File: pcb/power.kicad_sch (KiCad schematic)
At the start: 24 parts, among them J2 SM02B-SRSS-TB, Q1 2N7002, Q2 BSS84, SW1 SSSS211603, U2 TPS2112APW, U3 MCP73831-5-OT, U4 TLV70233DBVT

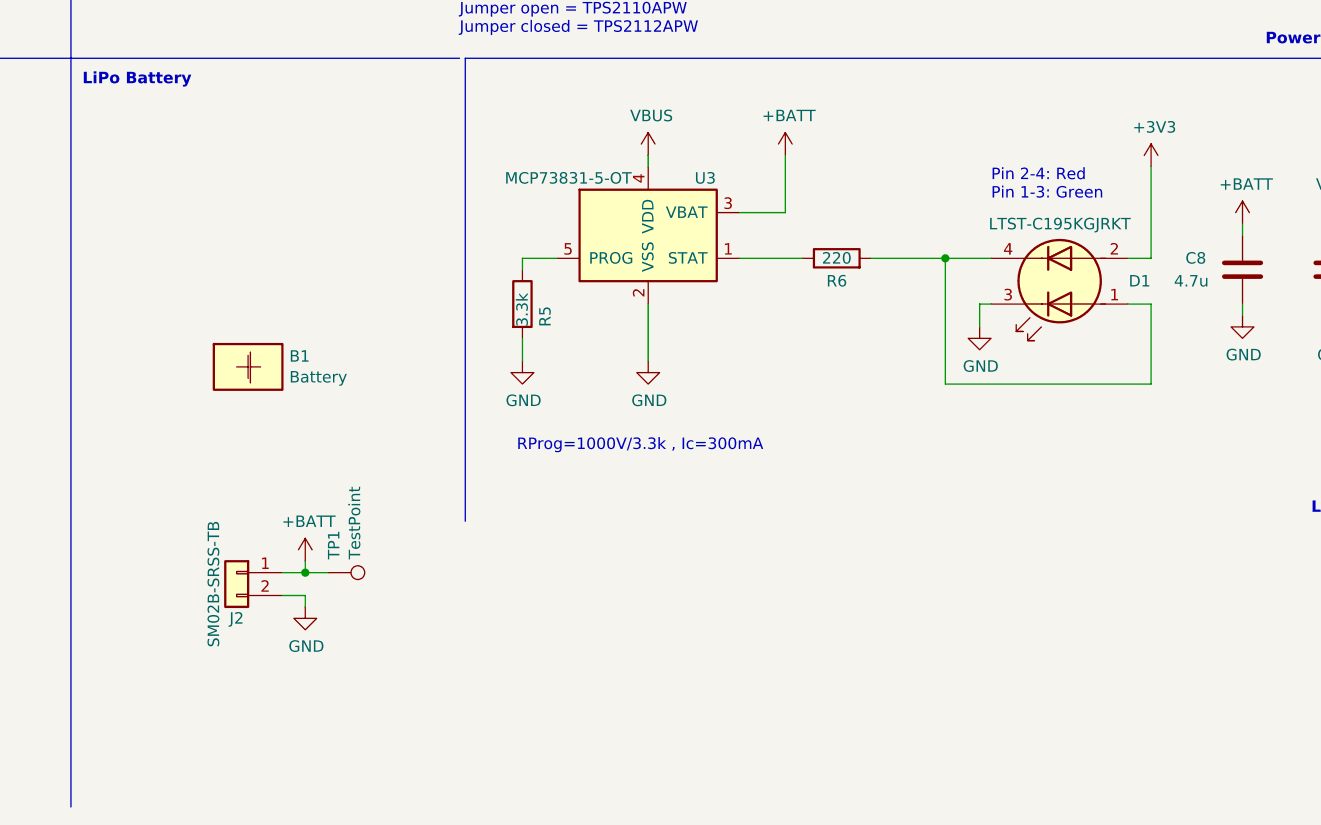
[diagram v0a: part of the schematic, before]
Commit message: Fix ERC warnings
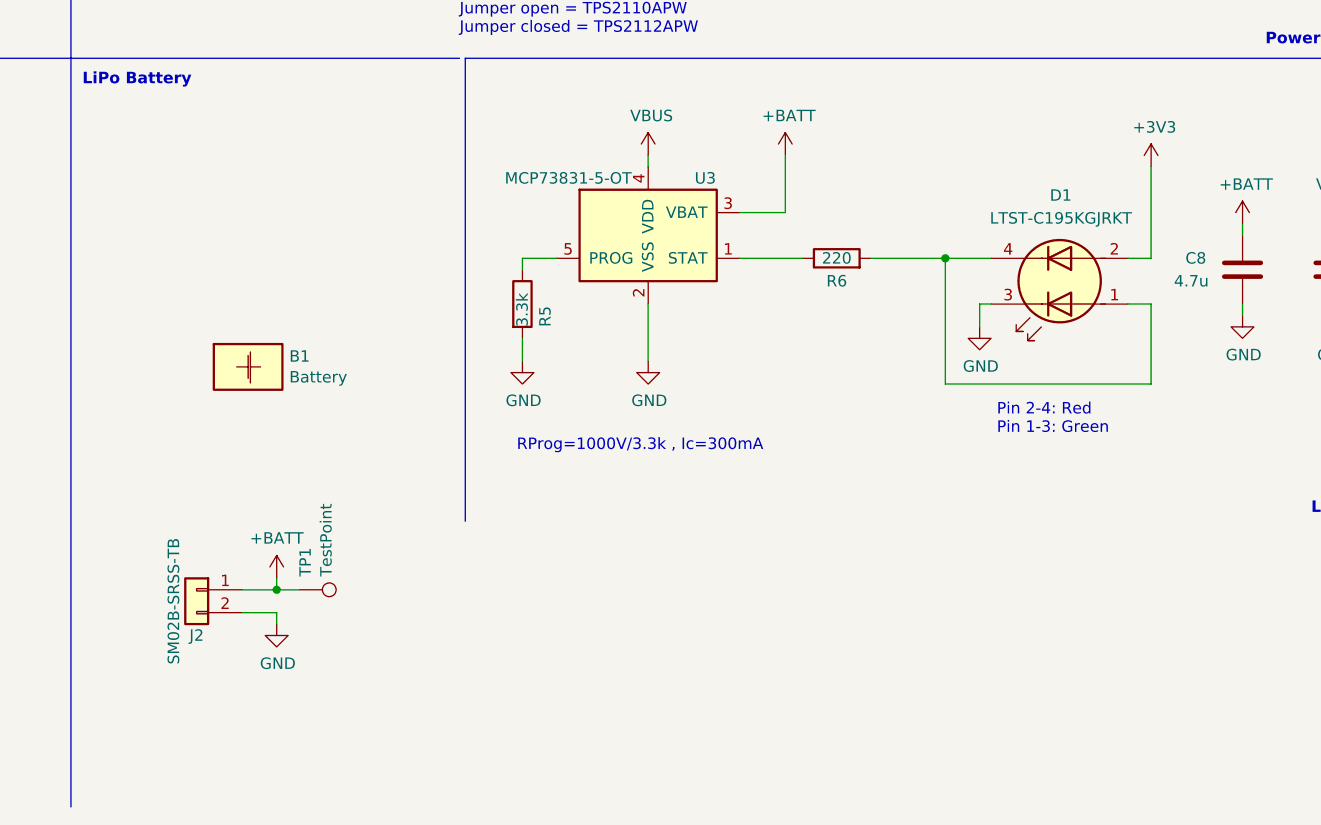
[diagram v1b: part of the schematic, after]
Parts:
- removed D1: LTST-C195KGJRKT, ultramote:LTST-C195KGJRKT, symbol ultramote-rescue:LED_Dual_AACC-Device
- added D1: LTST-C195KGJRKT, ultramote:LTST-C195KGJRKT, symbol Device:LED_Dual_AAKK
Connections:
- net +3V3: now also D1.2 (A2)
- net GND: now also D1.3 (K1)
- net at R6.2: now also D1.1 (A1), D1.4 (K2)
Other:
- moved on the sheet: J2, TP1
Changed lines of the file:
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@@
   (junction (at 189.23 73.66) (diameter 0) (color 0 0 0 0)
   )
-  (junction (at 159.385 171.45) (diameter 0) (color 0 0 0 0)
+  (junction (at 156.21 173.355) (diameter 0) (color 0 0 0 0)
   )
   (junction (at 144.78 53.34) (diameter 0) (color 0 0 0 0)
@@
   (junction (at 219.71 50.8) (diameter 0) (color 0 0 0 0)
   )
-  (wire (pts (xy 156.845 173.99) (xy 159.385 173.99))
+  (wire (pts (xy 152.4 175.895) (xy 156.21 175.895))
     (stroke (width 0) (type default) (color 0 0 0 0))
   )
@@
     (stroke (width 0) (type default) (color 0 0 0 0))
   )
-  (wire (pts (xy 159.385 171.45) (xy 156.845 171.45))
-    (stroke (width 0) (type default) (color 0 0 0 0))
-  )
   (wire (pts (xy 203.2 53.34) (xy 203.2 63.5))
     (stroke (width 0) (type default) (color 0 0 0 0))
@@
     (stroke (width 0) (type default) (color 0 0 0 0))
   )
+  (wire (pts (xy 152.4 173.355) (xy 156.21 173.355))
+    (stroke (width 0) (type default) (color 0 0 0 0))
+  )
   (wire (pts (xy 179.07 62.23) (xy 170.18 62.23))
     (stroke (width 0) (type default) (color 0 0 0 0))
@@
     (stroke (width 0) (type default) (color 0 0 0 0))
   )
-  (wire (pts (xy 161.925 171.45) (xy 159.385 171.45))
+  (wire (pts (xy 158.75 173.355) (xy 156.21 173.355))
     (stroke (width 0) (type default) (color 0 0 0 0))
   )
@@
     (stroke (width 0) (type default) (color 0 0 0 0))
   )
-  (wire (pts (xy 159.385 170.18) (xy 159.385 171.45))
+  (wire (pts (xy 156.21 172.085) (xy 156.21 173.355))
     (stroke (width 0) (type default) (color 0 0 0 0))
   )
@@
     (stroke (width 0) (type default) (color 0 0 0 0))
   )
-  (wire (pts (xy 159.385 173.99) (xy 159.385 175.26))
+  (wire (pts (xy 156.21 175.895) (xy 156.21 177.165))
     (stroke (width 0) (type default) (color 0 0 0 0))
   )
@@
     (effects (font (size 1.27 1.27) (thickness 0.254) bold) (justify left bottom))
   )
-  (text "Pin 2-4: Red\nPin 1-3: Green" (at 235.585 130.175 0)
+  (text "Pin 2-4: Red\nPin 1-3: Green" (at 236.22 156.21 0)
     (effects (font (size 1.27 1.27)) (justify left bottom))
   )
@@
     (pin "2")
   )
-  (symbol (lib_id "Connector_Generic:Conn_01x02") (at 151.765 171.45 0) (mirror y) (unit 1)
-    (in_bom yes) (on_board yes)
-    (property "Reference" "J2" (id 0) (at 151.765 176.53 0))
-    (property "Value" "SM02B-SRSS-TB" (id 1) (at 149.225 172.72 90))
-    (property "Footprint" "Connector_JST:JST_PH_B2B-PH-SM4-TB_1x02-1MP_P2.00mm_Vertical" (id 2) (at 151.765 171.45 0)
-      (effects (font (size 1.27 1.27)) hide)
-    )
-    (property "Datasheet" "~" (id 3) (at 151.765 171.45 0)
-      (effects (font (size 1.27 1.27)) hide)
-    )
-    (property "LCSC Part Number" "C160402" (id 4) (at 151.765 171.45 0)
-      (effects (font (size 1.27 1.27)) hide)
-    )
-    (property "Manufacturer Part Number" "S2B-PH-SM4-TB(LF)(SN)" (id 5) (at 151.765 171.45 0)
+  (symbol (lib_id "Connector_Generic:Conn_01x02") (at 147.32 173.355 0) (mirror y) (unit 1)
+    (in_bom yes) (on_board yes)
+    (property "Reference" "J2" (id 0) (at 147.32 178.435 0))
+    (property "Value" "SM02B-SRSS-TB" (id 1) (at 144.78 174.625 90))
+    (property "Footprint" "Connector_JST:JST_PH_B2B-PH-SM4-TB_1x02-1MP_P2.00mm_Vertical" (id 2) (at 147.32 173.355 0)
+      (effects (font (size 1.27 1.27)) hide)
+    )
+    (property "Datasheet" "~" (id 3) (at 147.32 173.355 0)
+      (effects (font (size 1.27 1.27)) hide)
+    )
+    (property "LCSC Part Number" "C160402" (id 4) (at 147.32 173.355 0)
+      (effects (font (size 1.27 1.27)) hide)
+    )
+    (property "Manufacturer Part Number" "S2B-PH-SM4-TB(LF)(SN)" (id 5) (at 147.32 173.355 0)
       (effects (font (size 1.27 1.27)) hide)
     )
@@
     )
     (pin "1")
-  )
-  (symbol (lib_id "ultramote-rescue:LED_Dual_AACC-Device") (at 243.205 139.065 180) (unit 1)
-    (in_bom yes) (on_board yes)
-    (property "Reference" "D1" (id 0) (at 252.095 139.065 0))
-    (property "Value" "LTST-C195KGJRKT" (id 1) (at 243.205 132.715 0))
-    (property "Footprint" "ultramote:LTST-C195KGJRKT" (id 2) (at 242.443 139.065 0)
-      (effects (font (size 1.27 1.27)) hide)
-    )
-    (property "Datasheet" "~" (id 3) (at 242.443 139.065 0)
-      (effects (font (size 1.27 1.27)) hide)
-    )
-    (property "LCSC Part Number" "C125104" (id 4) (at 243.205 139.065 0)
-      (effects (font (size 1.27 1.27)) hide)
-    )
-    (property "Manufacturer Part Number" "LTST-C195KGJRKT" (id 5) (at 243.205 139.065 0)
-      (effects (font (size 1.27 1.27)) hide)
-    )
-    (pin "1")
-    (pin "2")
-    (pin "3")
-    (pin "4")
   )
   (symbol (lib_id "power:+3V3") (at 254 48.26 0) (unit 1)
@@
     (pin "1")
   )
-  (symbol (lib_id "power:GND") (at 159.385 175.26 0) (unit 1)
-    (in_bom yes) (on_board yes)
-    (property "Reference" "#PWR018" (id 0) (at 159.385 181.61 0)
-      (effects (font (size 1.27 1.27)) hide)
-    )
-    (property "Value" "GND" (id 1) (at 159.512 179.6542 0))
-    (property "Footprint" "" (id 2) (at 159.385 175.26 0)
-      (effects (font (size 1.27 1.27)) hide)
-    )
-    (property "Datasheet" "" (id 3) (at 159.385 175.26 0)
+  (symbol (lib_id "power:GND") (at 156.21 177.165 0) (unit 1)
+    (in_bom yes) (on_board yes)
+    (property "Reference" "#PWR018" (id 0) (at 156.21 183.515 0)
+      (effects (font (size 1.27 1.27)) hide)
+    )
+    (property "Value" "GND" (id 1) (at 156.337 181.5592 0))
+    (property "Footprint" "" (id 2) (at 156.21 177.165 0)
+      (effects (font (size 1.27 1.27)) hide)
+    )
+    (property "Datasheet" "" (id 3) (at 156.21 177.165 0)
       (effects (font (size 1.27 1.27)) hide)
     )
@@
     )
     (pin "1")
+  )
+  (symbol (lib_id "Device:LED_Dual_AAKK") (at 243.205 139.065 180) (unit 1)
+    (in_bom yes) (on_board yes)
+    (property "Reference" "D1" (id 0) (at 243.332 129.54 0))
+    (property "Value" "LTST-C195KGJRKT" (id 1) (at 243.332 132.08 0))
+    (property "Footprint" "ultramote:LTST-C195KGJRKT" (id 2) (at 242.443 139.065 0)
+      (effects (font (size 1.27 1.27)) hide)
+    )
+    (property "Datasheet" "~" (id 3) (at 242.443 139.065 0)
+      (effects (font (size 1.27 1.27)) hide)
+    )
+    (property "LCSC Part Number" "C125104" (id 4) (at 243.205 139.065 0)
+      (effects (font (size 1.27 1.27)) hide)
+    )
+    (property "Manufacturer Part Number" "LTST-C195KGJRKT" (id 5) (at 243.205 139.065 0)
+      (effects (font (size 1.27 1.27)) hide)
+    )
+    (pin "1")
+    (pin "2")
+    (pin "3")
+    (pin "4")
   )
   (symbol (lib_id "Device:C") (at 74.93 162.56 0) (unit 1)
@@
     (pin "2")
   )
-  (symbol (lib_id "power:+BATT") (at 159.385 170.18 0) (unit 1)
-    (in_bom yes) (on_board yes)
-    (property "Reference" "#PWR017" (id 0) (at 159.385 173.99 0)
-      (effects (font (size 1.27 1.27)) hide)
-    )
-    (property "Value" "+BATT" (id 1) (at 159.766 165.7858 0))
-    (property "Footprint" "" (id 2) (at 159.385 170.18 0)
-      (effects (font (size 1.27 1.27)) hide)
-    )
-    (property "Datasheet" "" (id 3) (at 159.385 170.18 0)
+  (symbol (lib_id "power:+BATT") (at 156.21 172.085 0) (unit 1)
+    (in_bom yes) (on_board yes)
+    (property "Reference" "#PWR017" (id 0) (at 156.21 175.895 0)
+      (effects (font (size 1.27 1.27)) hide)
+    )
+    (property "Value" "+BATT" (id 1) (at 156.21 167.64 0))
+    (property "Footprint" "" (id 2) (at 156.21 172.085 0)
+      (effects (font (size 1.27 1.27)) hide)
+    )
+    (property "Datasheet" "" (id 3) (at 156.21 172.085 0)
       (effects (font (size 1.27 1.27)) hide)
     )
@@
     (pin "5")
   )
-  (symbol (lib_id "Connector:TestPoint") (at 161.925 171.45 270) (unit 1)
-    (in_bom yes) (on_board yes)
-    (property "Reference" "TP1" (id 0) (at 162.5854 169.9768 0)
+  (symbol (lib_id "Connector:TestPoint") (at 158.75 173.355 270) (unit 1)
+    (in_bom yes) (on_board yes)
+    (property "Reference" "TP1" (id 0) (at 159.4104 171.8818 0)
       (effects (font (size 1.27 1.27)) (justify right))
     )
-    (property "Value" "TestPoint" (id 1) (at 164.8968 169.9768 0)
+    (property "Value" "TestPoint" (id 1) (at 161.7218 171.8818 0)
       (effects (font (size 1.27 1.27)) (justify right))
     )
-    (property "Footprint" "TestPoint:TestPoint_Pad_1.0x1.0mm" (id 2) (at 161.925 176.53 0)
-      (effects (font (size 1.27 1.27)) hide)
-    )
-    (property "Datasheet" "~" (id 3) (at 161.925 176.53 0)
-      (effects (font (size 1.27 1.27)) hide)
-    )
+    (property "Footprint" "TestPoint:TestPoint_Pad_1.0x1.0mm" (id 2) (at 158.75 178.435 0)
+      (effects (font (size 1.27 1.27)) hide)
+    )
+    (property "Datasheet" "~" (id 3) (at 158.75 178.435 0)
+      (effects (font (size 1.27 1.27)) hide)
+    )

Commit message: Add datasheet links
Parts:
- J2: footprint Connector_JST:JST_PH_B2B-PH-SM4-TB_1x02-1MP_P2.00mm_Vertical -> Connector_JST:JST_SH_SM02B-SRSS-TB_1x02-1MP_P1.00mm_Horizontal
- U3: LCSC Part Number C424093 -> C424093
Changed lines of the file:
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@@
     (property "Reference" "J2" (id 0) (at 147.32 178.435 0))
     (property "Value" "SM02B-SRSS-TB" (id 1) (at 144.78 174.625 90))
-    (property "Footprint" "Connector_JST:JST_PH_B2B-PH-SM4-TB_1x02-1MP_P2.00mm_Vertical" (id 2) (at 147.32 173.355 0)
-      (effects (font (size 1.27 1.27)) hide)
-    )
-    (property "Datasheet" "~" (id 3) (at 147.32 173.355 0)
+    (property "Footprint" "Connector_JST:JST_SH_SM02B-SRSS-TB_1x02-1MP_P1.00mm_Horizontal" (id 2) (at 147.32 173.355 0)
+      (effects (font (size 1.27 1.27)) hide)
+    )
+    (property "Datasheet" "https://datasheet.lcsc.com/lcsc/1811151533_JST-Sales-America-SM02B-SRSS-TB-LF-SN_C160402.pdf" (id 3) (at 147.32 173.355 0)
       (effects (font (size 1.27 1.27)) hide)
     )
@@
       (effects (font (size 1.27 1.27)) hide)
     )
-    (property "Datasheet" "~" (id 3) (at 44.45 31.115 0)
+    (property "Datasheet" "https://datasheet.lcsc.com/lcsc/1805291752_ALPSALPINE-SSSS211603_C125040.pdf" (id 3) (at 44.45 31.115 0)
       (effects (font (size 1.27 1.27)) hide)
     )
@@
       (effects (font (size 1.27 1.27)) hide)
     )
-    (property "Datasheet" "~" (id 3) (at 242.443 139.065 0)
+    (property "Datasheet" "https://datasheet.lcsc.com/lcsc/1811100910_Lite-On-LTST-C195KGJRKT_C125104.pdf" (id 3) (at 242.443 139.065 0)
       (effects (font (size 1.27 1.27)) hide)
     )
@@
       (effects (font (size 1.27 1.27)) hide)
     )
-    (property "Datasheet" "" (id 3) (at 153.035 148.59 0)
+    (property "Datasheet" "~" (id 3) (at 153.035 148.59 0)
       (effects (font (size 1.27 1.27)) hide)
     )
@@
       (effects (font (size 1.27 1.27)) hide)
     )
-    (property "Datasheet" "" (id 3) (at 185.42 62.23 0)
+    (property "Datasheet" "https://www.ti.com/lit/ds/symlink/tps2113a.pdf?ts=1675422974516&ref_url=https%253A%252F%252Fwww.google.com%252F" (id 3) (at 185.42 62.23 0)
       (effects (font (size 1.27 1.27)) hide)
     )
@@
       (effects (font (size 1.27 1.27)) hide)
     )
-    (property "LCSC Part Number" " C424093" (id 4) (at 197.485 133.985 0)
-      (effects (font (size 1.27 1.27)) hide)
-    )
+    (property "LCSC Part Number" "C424093" (id 4) (at 197.485 133.985 0)
+      (effects (font (size 1.27 1.27)) hide)
+    )

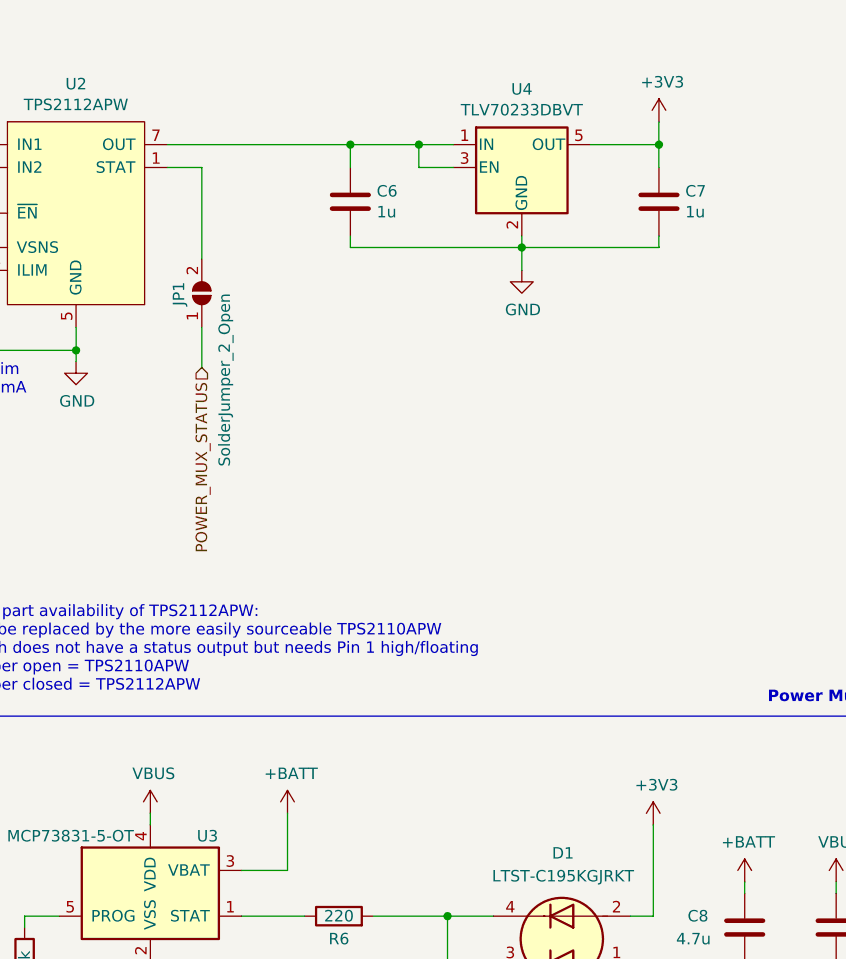
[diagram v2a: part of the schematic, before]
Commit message: Migrate project to KiCad v7
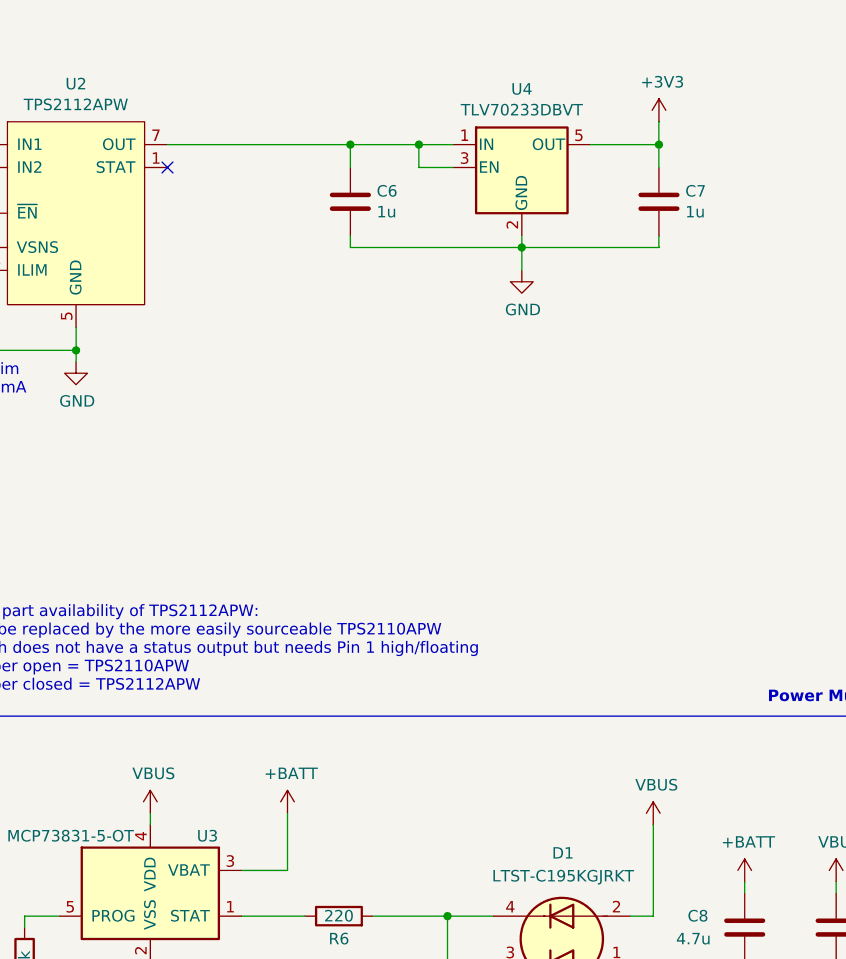
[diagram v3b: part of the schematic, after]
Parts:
- removed JP1: SolderJumper_2_Open, Jumper:SolderJumper-2_P1.3mm_Open_RoundedPad1.0x1.5mm, symbol Jumper:SolderJumper_2_Open
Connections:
- net +3V3: no longer D1.2 (A2)
- net VBUS: now also D1.2 (A2)
- no-connect marks 0 -> 1
